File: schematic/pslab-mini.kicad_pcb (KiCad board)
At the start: 4 copper layers, 85 x 56 mm, 150 parts, among them J1 USB_C_Receptacle_USB2.0_16P, J2 Battery_Cell, J3 Conn_Coaxial, J4 Conn_Coaxial, J5 Conn_02x18_Odd_Even, J6 Conn_01x15_Socket, J7 Conn_02x03_Top_Bottom, Q1 MMBT3904, Q2 MMBT3906, SW1 Reset, SW2 Power, U1 MT1470, U10 TL082, U11 ESP32-C3, U2 AP3015A, U3 IP5189T, U4 SP0503BAHT, U5 AMS1117-3.3, U6 STM32H563RIT6, U7 TL082, U8 MCP6S21, U9 MCP6S21, X1 32kHz768, Y1 Crystal_25MHz, Y2 Crystal_40Mhz

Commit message: fixup
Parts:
- R14, R15, R18, R20: footprint Resistor_SMD:R_0603_1608Metric -> Resistor_SMD:R_0402_1005Metric
- moved FID2 90.0 mm to (158.8, 55.2)
- moved SW2 62.4 mm to (142.0, 100.5), turned to 180 degrees
- moved C17 16.1 mm to (90.4, 71.7), turned to 0 degrees
- moved C35 13.9 mm to (86.6, 86.3), turned to 0 degrees
- moved C39 13.7 mm to (96.5, 86.5), turned to 0 degrees
- moved F1 11.7 mm to (147.8, 91.2)
- moved Y2 11.2 mm to (86.3, 89.3), turned to 0 degrees
- moved C36 11.0 mm to (83.1, 89.1), turned to -90 degrees
- moved R35 9.37 mm to (85.5, 92.0), turned to 0 degrees
- moved C43 9.36 mm to (97.8, 96.5), turned to 180 degrees
- moved SW1 9.35 mm to (84.7, 73.9)
- moved D10 9.32 mm to (151.3, 108.2), turned to 0 degrees
- moved D9 9.28 mm to (151.2, 106.3), turned to 180 degrees
- moved D8 9.25 mm to (151.2, 104.3), turned to 0 degrees
- moved C2 9.24 mm to (146.3, 93.8), turned to 0 degrees
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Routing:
- net Net-(NT4-Pad1): track 1.22 -> 0.00 mm
- net Net-(NT3-Pad1): track 1.15 -> 0.00 mm
- net Net-(NT2-Pad1): track 1.00 -> 0.00 mm
- net Net-(NT5-Pad1): track 1.00 -> 0.00 mm
- net Net-(NT1-Pad1): track 0.96 -> 0.00 mm

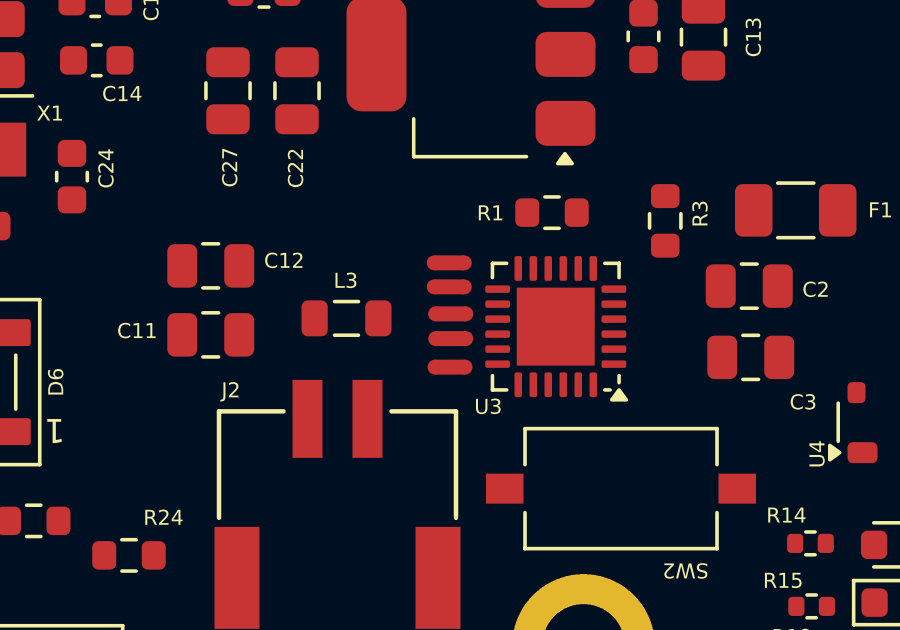
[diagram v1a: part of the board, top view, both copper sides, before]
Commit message: DRC and ERC fixes
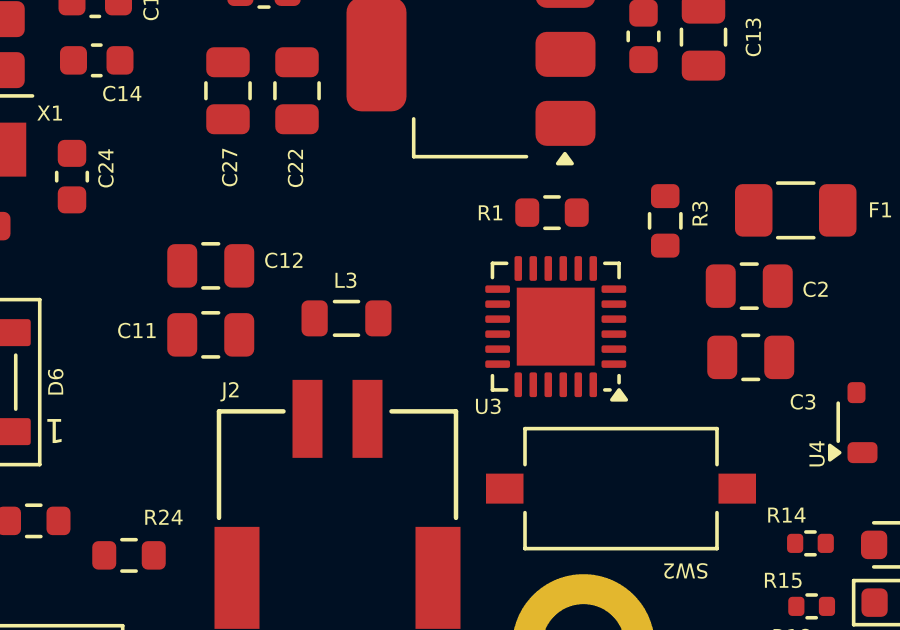
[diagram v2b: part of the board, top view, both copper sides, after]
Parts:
- removed NT1, NT2, NT3, NT4, NT5: NetTie_2, NetTie:NetTie-2_SMD_Pad0.5mm
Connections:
- U3 pad 13: Net-(NT3-Pad1) -> Net-(L3-Pad1)
- U3 pad 14: Net-(NT4-Pad1) -> Net-(L3-Pad1)
- U3 pad 15: Net-(NT5-Pad1) -> Net-(L3-Pad1)
- U3 pad 16: Net-(NT1-Pad1) -> +5V
- U3 pad 17: Net-(NT2-Pad1) -> +5V

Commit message: layout optimization
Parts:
- moved R29 43.9 mm to (137.7, 76.2)
- moved C1 39.6 mm to (115.5, 88.5), turned to 0 degrees
- moved U9 38.4 mm to (138.4, 70.6), turned to 90 degrees
- moved R2 37.1 mm to (115.5, 85.7), turned to 0 degrees
- moved R25 33.8 mm to (140.4, 63.1)
- moved U1 32.4 mm to (119.1, 85.5), turned to -90 degrees
- moved R30 31.5 mm to (144.0, 63.4), turned to 90 degrees
- moved R31 31.2 mm to (143.2, 74.7), turned to -90 degrees
- moved R6 30.4 mm to (118.4, 89.3), turned to 90 degrees
- moved TP3 30.0 mm to (125.8, 87.0)
- moved C4 29.2 mm to (122.0, 86.5), turned to -90 degrees
- moved R7 29.0 mm to (121.9, 89.7), turned to -90 degrees
- moved R28 28.0 mm to (140.5, 65.1)
- moved C6 27.9 mm to (120.1, 89.3), turned to 90 degrees
- moved U10 27.3 mm to (145.4, 68.9), turned to 90 degrees
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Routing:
- net /CH1: track 0.00 -> 39.2 mm, vias 0 -> 1
- net /SPI1_MOSI: track 0.00 -> 37.9 mm, vias 0 -> 3
- net /SPI1_SCK: track 0.00 -> 34.0 mm, vias 0 -> 2
- net /CS1: track 0.00 -> 29.7 mm, vias 0 -> 2
- net /CH2: track 0.00 -> 26.2 mm
- net /CH1_IN: track 0.00 -> 25.6 mm
- net /CS2: track 0.00 -> 25.3 mm
- net /CH2_IN: track 0.00 -> 18.3 mm
- net /OSC_REF1: track 0.00 -> 15.3 mm, vias 0 -> 2
- net Net-(U8-CHA): track 0.00 -> 12.5 mm
- net Net-(U7A-+): track 0.00 -> 12.3 mm
- net Net-(U9-CHA): track 0.00 -> 9.31 mm
- net Net-(U10A--): track 0.00 -> 7.75 mm
- net Net-(R28-Pad1): track 0.00 -> 5.57 mm
- net Net-(R31-Pad1): track 0.00 -> 5.07 mm
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
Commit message: updated routing
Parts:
- removed C45: 1.2pF, Capacitor_SMD:C_0603_1608Metric
- removed C9: 22uF, Capacitor_SMD:C_0805_2012Metric
- removed J1: USB_C_Receptacle_USB2.0_16P, pslab-mini:USB_C_Receptacle_G-Switch_GT-USB-7010ASV
- removed R18, R20: 200, Resistor_SMD:R_0402_1005Metric
- removed U3: IP5189T, Package_DFN_QFN:QFN-24-1EP_4x4mm_P0.5mm_EP2.6x2.6mm
- added D13: GREEN, LED_SMD:LED_0805_2012Metric, F.Cu at (145.5, 106.8)
- added J8: USB_C_Receptacle_USB2.0_16P, pslab-mini:USB_C_Receptacle_G-Switch_GT-USB-7010ASV, F.Cu at (160.8, 98.6)
- added L6: 2.7nH, Inductor_SMD:L_0402_1005Metric, F.Cu at (88.4, 89.5)
- added TP10: +5V, pslab-mini:Test_Point_0.8mm, F.Cu at (138.2, 102.0)
- added TP11: VIN, pslab-mini:Test_Point_0.8mm, F.Cu at (140.0, 102.2)
- added U12: IP5189T, Package_DFN_QFN:QFN-24-1EP_4x4mm_P0.5mm_EP2.6x2.6mm, F.Cu at (141.8, 99.0)
- C11: value 10uF -> 22uF
- C4: value 1uF -> 22nF
- C44: value 1.2pF -> 1pF; footprint Capacitor_SMD:C_0603_1608Metric -> Capacitor_SMD:C_0402_1005Metric
- D10: value White -> 100%
- D7: value White -> 25%
- D8: value White -> 50%
- D9: value White -> 75%
- J2: value Battery_Cell -> BAT
- J5: value Conn_02x18_Odd_Even -> Conn_02x16_Odd_Even; footprint Connector_PinSocket_2.54mm:PinSocket_2x18_P2.54mm_Vertical -> Connector_PinSocket_2.54mm:PinSocket_2x16_P2.54mm_Vertical
- L5: value 2.4nH -> 3.9nH
- PCB_ANT1: footprint Diode_SMD:D_1206_3216Metric -> RF_Antenna:Johanson_2450AT18x100
- R35, R37, R38, R39: footprint Resistor_SMD:R_0603_1608Metric -> Resistor_SMD:R_0402_1005Metric
- U1: value MT1470 -> MT2496
- moved R26 26.7 mm to (146.8, 57.2)
- moved C32 26.4 mm to (148.5, 57.2), turned to -90 degrees
- moved R27 21.4 mm to (140.2, 61.8), turned to 90 degrees
- moved U7 21.0 mm to (147.2, 62.2)
- moved C33 19.6 mm to (142.0, 61.8), turned to 90 degrees
- moved SW2 15.9 mm to (154.6, 90.9)
- moved C35 14.8 mm to (98.0, 83.8), turned to -90 degrees
- moved C36 14.7 mm to (94.2, 80.5)
- moved FLASH1 14.6 mm to (103.0, 92.0), turned to -90 degrees
- moved C37 14.4 mm to (91.0, 81.5), turned to 90 degrees
- moved R32 11.7 mm to (155.0, 70.8), turned to 180 degrees
- moved R39 11.4 mm to (99.8, 83.5)
- moved R38 11.2 mm to (101.5, 83.5)
- moved R37 11.1 mm to (103.2, 83.5)
- moved Y2 11.1 mm to (95.2, 84.2), turned to -90 degrees
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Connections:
- net /BAT+ renamed /BC_BATT
- net /VINPUT renamed VIN
- net /VUSBIN renamed VBUS
- C3 pad 1: Net-(U3-VDD) -> /BC_VDD
- C44 pad 2: GND -> Net-(C44-Pad2)
- D10 pad 1: Net-(D10-K) -> /BC_LED1
- D10 pad 2: /LD3 -> /BC_LED3R
- D7 pad 1: /LD3 -> /BC_LED3R
- D7 pad 2: Net-(D7-A) -> /BC_LED2
- D8 pad 1: Net-(D8-K) -> /BC_LED2
- D8 pad 2: /LD3 -> /BC_LED3R
- D9 pad 1: /LD3 -> /BC_LED3R
- D9 pad 2: Net-(D9-A) -> /BC_LED1
- J5 pad 1: Net-(J5-Pin_1) -> GND
- J5 pad 11: Net-(J5-Pin_1) -> GND
- J5 pad 13: Net-(J5-Pin_1) -> GND
- J5 pad 15: Net-(J5-Pin_1) -> GND
- J5 pad 17: Net-(J5-Pin_1) -> GND
- J5 pad 3: Net-(J5-Pin_1) -> GND
- J5 pad 32: /CH1 -> +5V
- J5 pad 5: Net-(J5-Pin_1) -> GND
- J5 pad 7: Net-(J5-Pin_1) -> GND
- J5 pad 9: Net-(J5-Pin_1) -> GND
- L3 pad 1: Net-(L3-Pad1) -> /LX
- L5 pad 2: /LNA_IN -> Net-(C44-Pad2)
- PCB_ANT1 pad 2: GND -> unconnected-(PCB_ANT1-Pad2)
- R1 pad 1: Net-(U3-ICHG) -> GND
- R1 pad 2: GND -> /BC_ICHG
- R14 pad 1: Net-(D7-A) -> /BC_LED3
- R14 pad 2: /LD2 -> /BC_LED3R
- R15 pad 1: Net-(D8-K) -> /BC_LED
- R15 pad 2: /LD2 -> Net-(D13-A)
- R3 pad 1: Net-(U3-NTC) -> GND
- R3 pad 2: GND -> /BC_NTC
- SW2 pad 2: /KEY -> /BC_KEY
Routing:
- net +3V3: track 0.00 -> 218.4 mm, vias 0 -> 10
- net VDDA: track 0.00 -> 143.8 mm, vias 0 -> 11
- net GND: track 0.00 -> 123.2 mm, vias 0 -> 84
- net +5V: track 0.00 -> 88.8 mm, vias 0 -> 3
- net /D-: track 0.00 -> 64.1 mm, vias 0 -> 2
- net /D+: track 0.00 -> 61.2 mm, vias 0 -> 2
- net -6V: track 0.00 -> 55.1 mm, vias 0 -> 3
- net /UART6_TX: track 0.00 -> 46.3 mm, vias 0 -> 1
- net /NRST: track 0.00 -> 45.2 mm
- net /UART6_RX: track 0.00 -> 44.1 mm, vias 0 -> 1
- net +6V: track 0.00 -> 35.2 mm, vias 0 -> 3
- net /ESP_DATA_READY: track 0.00 -> 34.3 mm, vias 0 -> 4
- net /I2C1_SDA: track 0.00 -> 33.6 mm, vias 0 -> 2
- net /SPI.CS: track 0.00 -> 32.6 mm
- net /SPI3_SCK: track 0.00 -> 32.2 mm
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- added copper zone on F.Cu, net GND
- added copper zone on In1.Cu, net GND
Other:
- board text added: "POWER"
- board text added: "RESET"
